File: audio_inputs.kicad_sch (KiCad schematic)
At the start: 14 parts, among them J2 PLR237/T10BK, U4 DIR9001PW

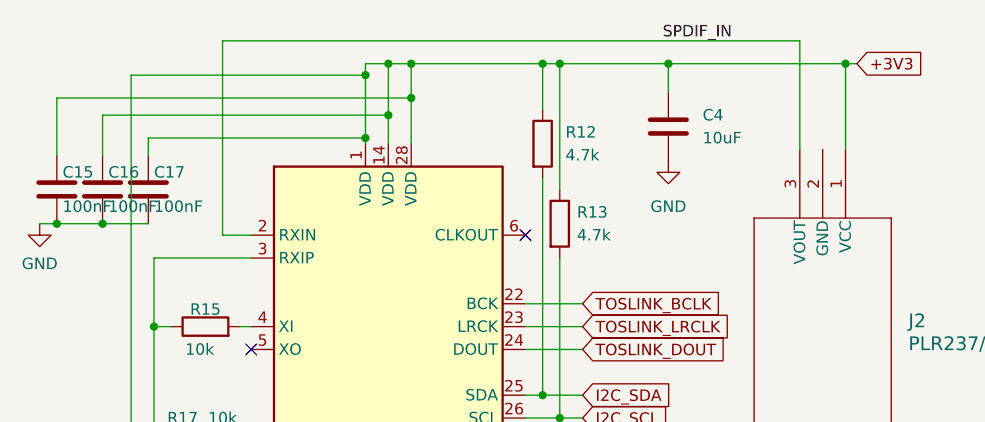
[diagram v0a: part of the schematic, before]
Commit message: Fixed RCA Jack symbols and footprints
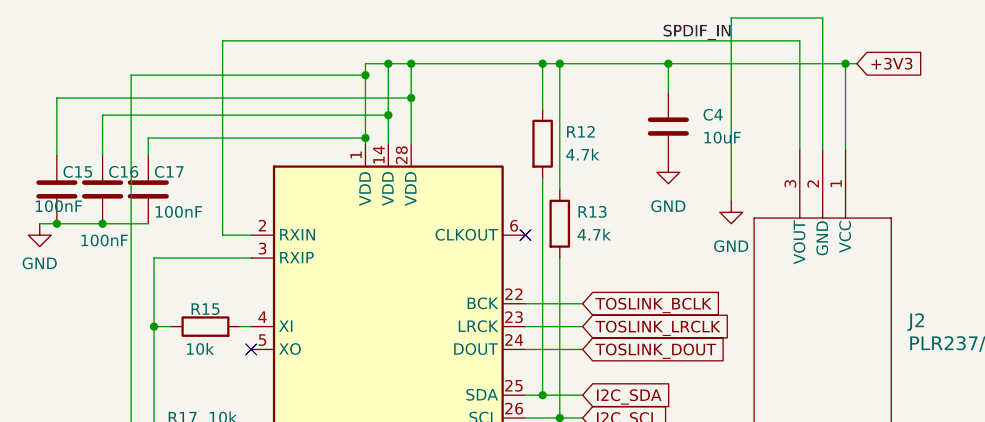
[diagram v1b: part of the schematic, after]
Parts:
- J2: footprint PLR237/T10BK_EVE -> Connector_Audio:PLR237-T10BK
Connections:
- net GND: now also J2.2 (GND)

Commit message: fixed cooper fill zone issue.  Fixed broken routes
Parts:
- J2: footprint Connector_Audio:PLR237-T10BK -> RCJ-042:PLR237T10BK
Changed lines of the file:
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@@
 			)
 		)
-		(property "Footprint" "Connector_Audio:PLR237-T10BK"
+		(property "Footprint" "RCJ-042:PLR237T10BK"
 			(at 136.525 57.785 0)
 			(effects

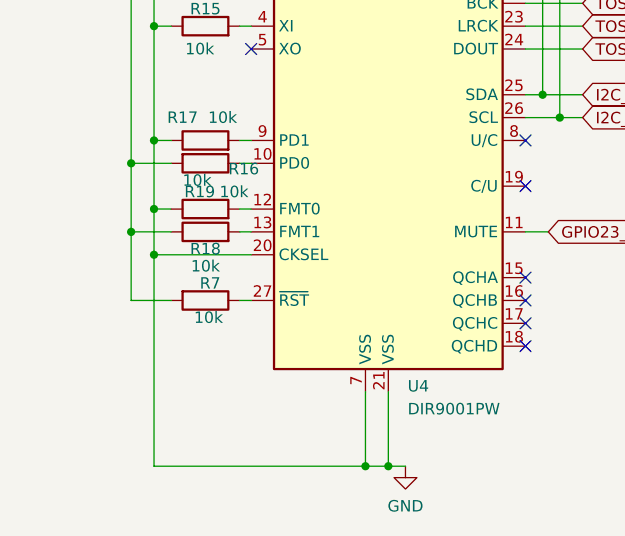
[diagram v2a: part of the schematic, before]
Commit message: Fixed inconsistencies in footprints and names
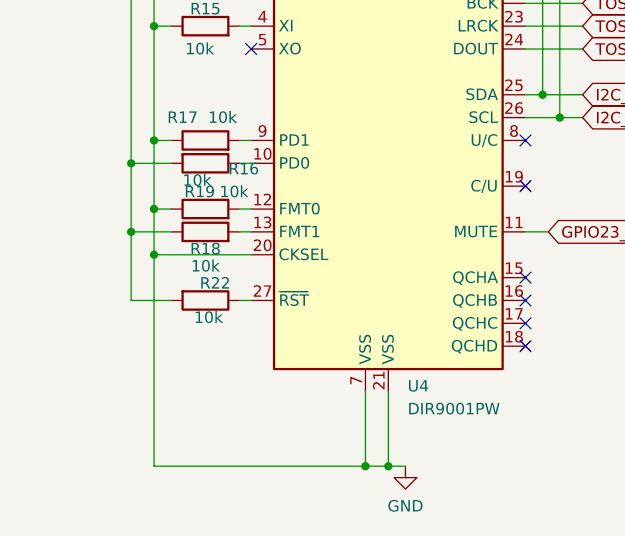
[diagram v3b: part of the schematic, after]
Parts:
- C4: footprint Resistor_SMD:R_0805_2012Metric_Pad1.20x1.40mm_HandSolder -> Capacitor_SMD:C_0805_2012Metric_Pad1.18x1.45mm_HandSolder
- renumbered R7 to R22
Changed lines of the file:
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@@
 		(on_board yes)
 		(dnp no)
-		(property "Reference" "R7"
+		(property "Reference" "R22"
 			(at 64.77 106.045 90)
 			(effects
@@
 			(project ""
 				(path "/e63e39d7-6ac0-4ffd-8aa3-1841a4541b55/69671d55-966b-4bba-8a79-dc8715674913"
-					(reference "R7")
+					(reference "R22")
 					(unit 1)
 				)
@@
 			)
 		)
-		(property "Footprint" "Resistor_SMD:R_0805_2012Metric_Pad1.20x1.40mm_HandSolder"
+		(property "Footprint" "Capacitor_SMD:C_0805_2012Metric_Pad1.18x1.45mm_HandSolder"
 			(at 117.8052 59.055 0)
 			(effects

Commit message: Removed unneeded crystal for DIR9001PW
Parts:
- U4: footprint Package_SO:SOIC-28W_7.5x17.9mm_P1.27mm -> Package_SO:TSSOP-28_4.4x9.7mm_P0.65mm
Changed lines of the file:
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@@
 			)
 		)
-		(property "Footprint" "Package_SO:SOIC-28W_7.5x17.9mm_P1.27mm"
+		(property "Footprint" "Package_SO:TSSOP-28_4.4x9.7mm_P0.65mm"
 			(at 85.725 119.38 0)
 			(effects

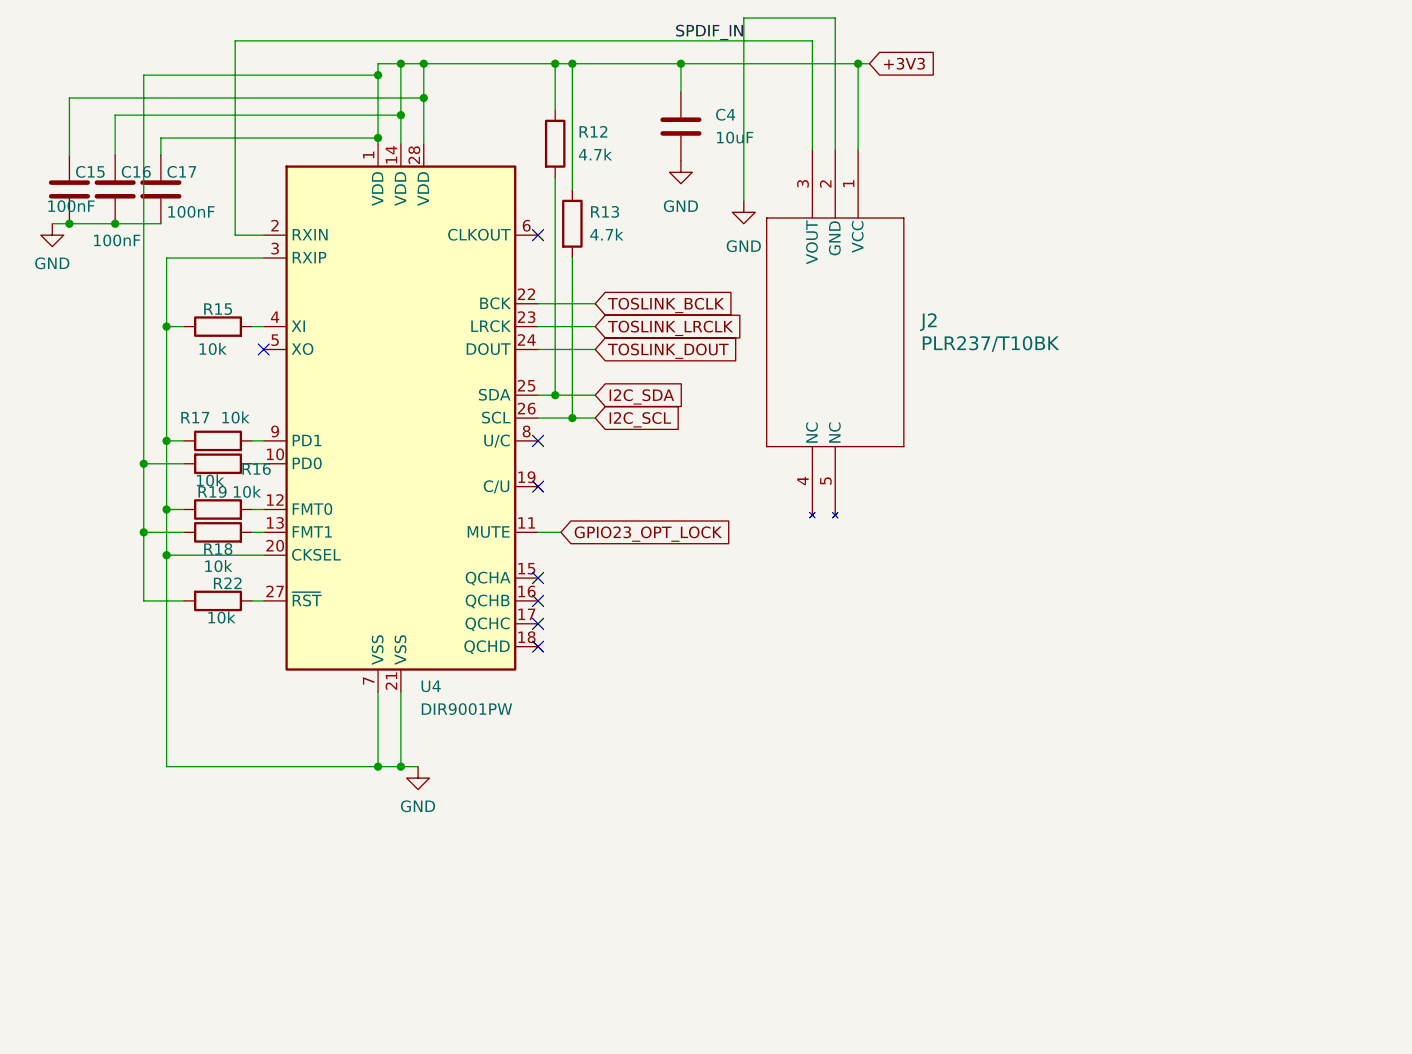
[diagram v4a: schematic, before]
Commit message: Updated schematic with correct symbol for DIR9001PW
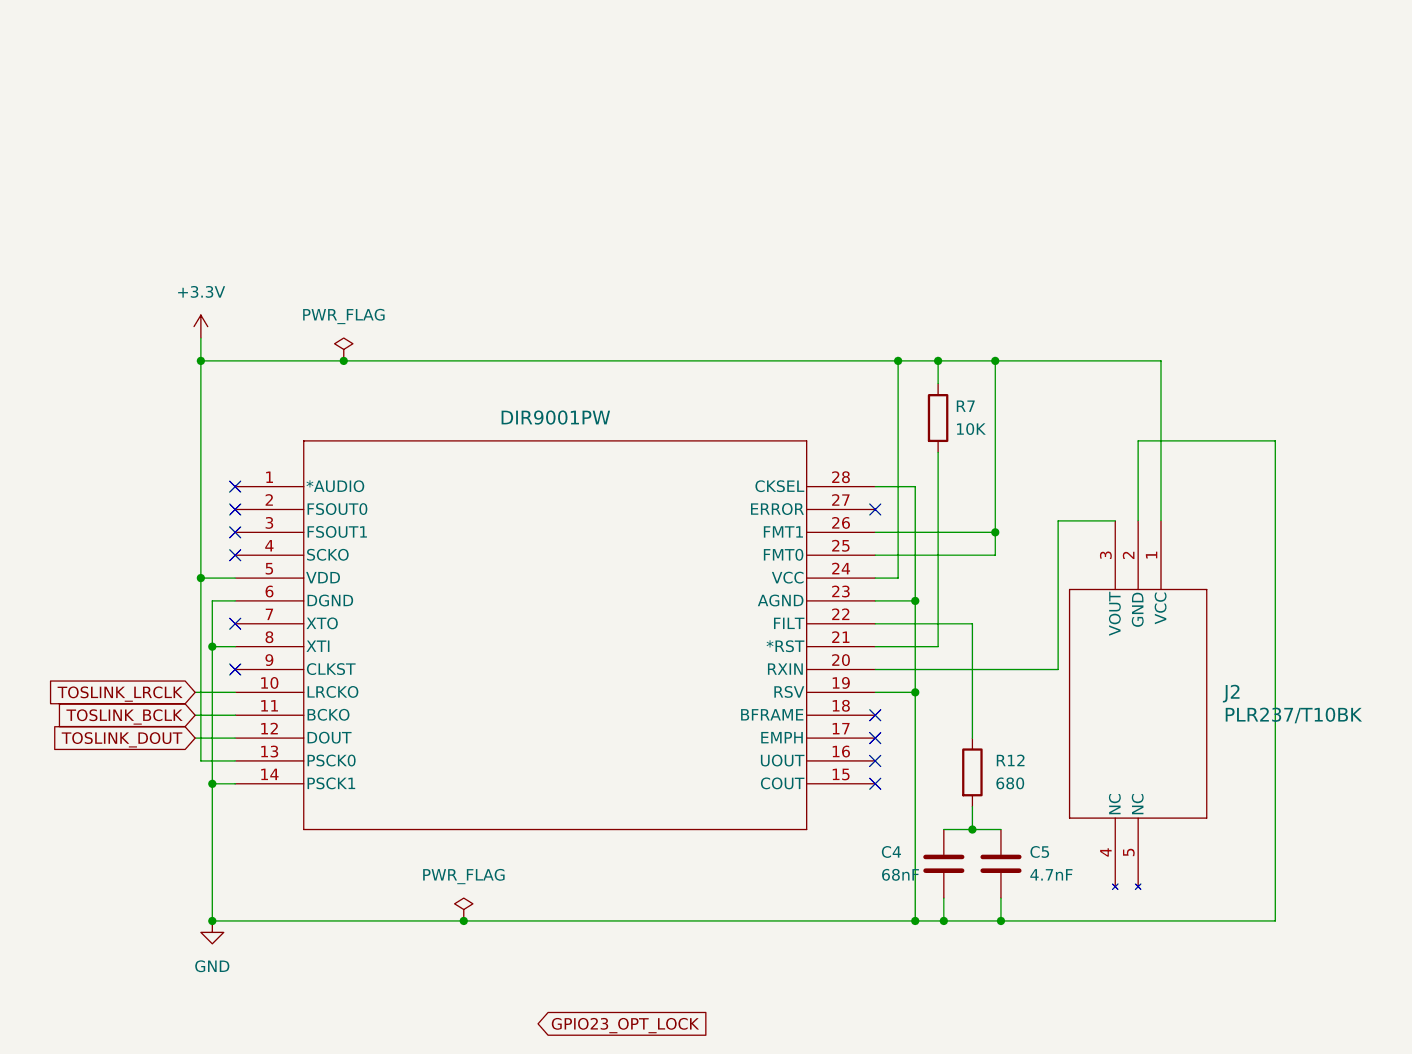
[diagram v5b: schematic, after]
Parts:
- removed C15, C16, C17: 100nF, Capacitor_SMD:C_0805_2012Metric_Pad1.18x1.45mm_HandSolder, symbol Device:C
- removed R13: 4.7k, Resistor_SMD:R_0805_2012Metric_Pad1.20x1.40mm_HandSolder, symbol Device:R
- removed R15, R16, R17, R18, R19, R22: 10k, Resistor_SMD:R_0805_2012Metric_Pad1.20x1.40mm_HandSolder, symbol Device:R
- removed U4: DIR9001PW, Package_SO:TSSOP-28_4.4x9.7mm_P0.65mm, symbol DIR9001:DIR9001PW
- added C5: 4.7nF, symbol Device:C
- added R7: 10K, symbol Device:R
- added U5: DIR9001PW, DIR9001_newfoot:PW28-M, symbol DIR9001:DIR9001PW
- C4: value 10uF -> 68nF; footprint Capacitor_SMD:C_0805_2012Metric_Pad1.18x1.45mm_HandSolder -> (none)
- R12: value 4.7k -> 680; footprint Resistor_SMD:R_0805_2012Metric_Pad1.20x1.40mm_HandSolder -> (none)
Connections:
- net GND: now also C5.2, U5.14 (PSCK1), U5.19 (RSV), U5.23 (AGND), U5.28 (CKSEL), U5.6 (DGND), U5.8 (XTI)
- net TOSLINK_BCLK: now also U5.11 (BCKO)
- net TOSLINK_DOUT: now also U5.12 (DOUT)
- net TOSLINK_LRCLK: now also U5.10 (LRCKO)
- removed net +3V3: C4.1, J2.1 (VCC), R12.1
- net I2C_SDA: no longer names the net of R12.2
- net I2C_SDA: now also C4.1, C5.1
- net SPDIF_IN: no longer names the net of J2.3 (VOUT)
- net SPDIF_IN: now also U5.20 (RXIN)
- new net: R7.2, U5.21 (*RST)
- new net: R12.1, U5.22 (FILT)
- new net +3.3V: J2.1 (VCC), R7.1, U5.13 (PSCK0), U5.24 (VCC), U5.25 (FMT0), U5.26 (FMT1), U5.5 (VDD)
- no-connect marks 8 -> 11
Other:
- moved on the sheet: J2

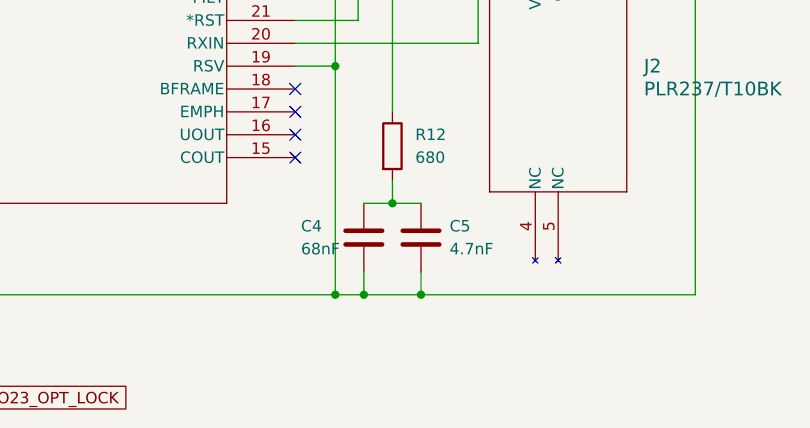
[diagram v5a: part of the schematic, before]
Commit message: Progress updating to correct footprint for DIR9001PW chip
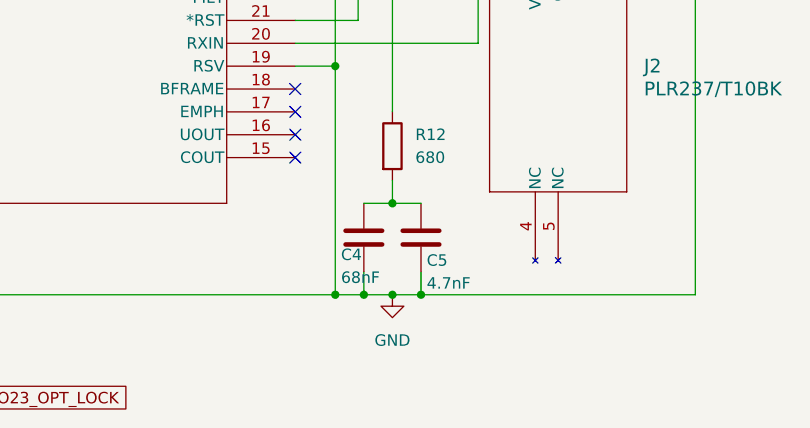
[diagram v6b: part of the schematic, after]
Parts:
- C4, C5: footprint (none) -> Capacitor_SMD:C_0805_2012Metric_Pad1.18x1.45mm_HandSolder
- R12, R7: footprint (none) -> Resistor_SMD:R_0805_2012Metric_Pad1.20x1.40mm_HandSolder
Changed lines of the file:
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@@
+	)
+	(junction
+		(at 149.225 143.51)
+		(diameter 0)
+		(color 0 0 0 0)
 	)
 	(junction
@@
 	(wire
 		(pts
-			(xy 146.05 143.51) (xy 152.4 143.51)
+			(xy 146.05 143.51) (xy 149.225 143.51)
 		)
 		(stroke
@@
 		(pts
 			(xy 92.71 143.51) (xy 142.875 143.51)
+		)
+		(stroke
+			(width 0)
+			(type default)
+		)
+	)
+	(wire
+		(pts
+			(xy 149.225 143.51) (xy 152.4 143.51)
 		)
 		(stroke
@@
 		(on_board yes)
 		(dnp no)
-		(fields_autoplaced yes)
 		(property "Reference" "#PWR06"
 			(at 64.77 149.86 0)
@@
 			)
 		)
-		(property "Footprint" ""
+		(property "Footprint" "Resistor_SMD:R_0805_2012Metric_Pad1.20x1.40mm_HandSolder"
 			(at 147.447 127 90)
 			(effects
@@
 			)
 		)
-		(property "Footprint" ""
+		(property "Footprint" "Resistor_SMD:R_0805_2012Metric_Pad1.20x1.40mm_HandSolder"
 			(at 143.637 87.63 90)
 			(effects
@@
 		(on_board yes)
 		(dnp no)
-		(fields_autoplaced yes)
 		(property "Reference" "C5"
-			(at 155.575 135.8899 0)
+			(at 153.035 139.7 0)
 			(effects
 				(font
@@
 		)
 		(property "Value" "4.7nF"
-			(at 155.575 138.4299 0)
+			(at 153.035 142.24 0)
 			(effects
 				(font
@@
 			)
 		)
-		(property "Footprint" ""
+		(property "Footprint" "Capacitor_SMD:C_0805_2012Metric_Pad1.18x1.45mm_HandSolder"
 			(at 153.3652 140.97 0)
 			(effects
@@
 				(path "/e63e39d7-6ac0-4ffd-8aa3-1841a4541b55/69671d55-966b-4bba-8a79-dc8715674913"
 					(reference "C5")
+					(unit 1)
+				)
+			)
+		)
+	)
+	(symbol
+		(lib_id "power:GND")
+		(at 149.225 143.51 0)
+		(unit 1)
+		(exclude_from_sim no)
+		(in_bom yes)
+		(on_board yes)
+		(dnp no)
+		(fields_autoplaced yes)
+		(property "Reference" "#PWR08"
+			(at 149.225 149.86 0)
+			(effects
+				(font
+					(size 1.27 1.27)
+				)
+				(hide yes)
+			)
+		)
+		(property "Value" "GND"
+			(at 149.225 148.59 0)
+			(effects
+				(font
+					(size 1.27 1.27)
+				)
+			)
+		)
+		(property "Footprint" ""
+			(at 149.225 143.51 0)
+			(effects
+				(font
+					(size 1.27 1.27)
+				)
+				(hide yes)
+			)
+		)
+		(property "Datasheet" ""
+			(at 149.225 143.51 0)
+			(effects
+				(font
+					(size 1.27 1.27)
+				)
+				(hide yes)
+			)
+		)
+		(property "Description" "Power symbol creates a global label with name \"GND\" , ground"
+			(at 149.225 143.51 0)
+			(effects
+				(font
+					(size 1.27 1.27)
+				)
+				(hide yes)
+			)
+		)
+		(pin "1"
+		)
+		(instances
+			(project ""
+				(path "/e63e39d7-6ac0-4ffd-8aa3-1841a4541b55/69671d55-966b-4bba-8a79-dc8715674913"
+					(reference "#PWR08")
 					(unit 1)
 				)
@@
 		(dnp no)
 		(property "Reference" "C4"
-			(at 139.065 135.89 0)
+			(at 143.51 139.065 0)
 			(effects
 				(font
@@
 		)
 		(property "Value" "68nF"
-			(at 139.065 138.43 0)
+			(at 143.51 141.605 0)
 			(effects
 				(font
@@
 			)
 		)
-		(property "Footprint" ""
+		(property "Footprint" "Capacitor_SMD:C_0805_2012Metric_Pad1.18x1.45mm_HandSolder"
 			(at 147.0152 140.97 0)
 			(effects

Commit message: kinda broken
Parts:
- renumbered C4 to C18, C5 to C19
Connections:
- net TOSLINK Error: now reaches U5.27 (ERROR)
- no-connect marks 11 -> 10
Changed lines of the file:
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@@
-	)
-	(no_connect
-		(at 138.43 97.79)
 	)
 	(no_connect
@@
 	(wire
 		(pts
-			(xy 158.75 115.57) (xy 158.75 99.06)
+			(xy 156.845 115.57) (xy 156.845 99.06)
 		)
 		(stroke
@@
 	(wire
 		(pts
-			(xy 138.43 115.57) (xy 158.75 115.57)
+			(xy 138.43 115.57) (xy 156.845 115.57)
 		)
 		(stroke
@@
 	(wire
 		(pts
-			(xy 158.75 99.06) (xy 165.1 99.06)
+			(xy 156.845 99.06) (xy 165.1 99.06)
 		)
 		(stroke
@@
 	(wire
 		(pts
+			(xy 138.43 97.79) (xy 140.335 97.79)
+		)
+		(stroke
+			(width 0)
+			(type default)
+		)
+	)
+	(wire
+		(pts
 			(xy 149.225 143.51) (xy 152.4 143.51)
 		)
@@
 			(width 0)
 			(type default)
-		)
-	)
-	(global_label "GPIO23_OPT_LOCK"
-		(shape input)
-		(at 100.965 154.94 0)
-		(fields_autoplaced yes)
-		(effects
-			(font
-				(size 1.27 1.27)
-			)
-			(justify left)
-		)
-		(property "Intersheetrefs" "${INTERSHEET_REFS}"
-			(at 121.3415 154.94 0)
-			(effects
-				(font
-					(size 1.27 1.27)
-				)
-				(justify left)
-				(hide yes)
-			)
 		)
 	)
@@
 				)
 				(justify right)
+				(hide yes)
+			)
+		)
+	)
+	(global_label "TOSLINK Error"
+		(shape input)
+		(at 140.335 97.79 0)
+		(fields_autoplaced yes)
+		(effects
+			(font
+				(size 1.27 1.27)
+			)
+			(justify left)
+		)
+		(property "Intersheetrefs" "${INTERSHEET_REFS}"
+			(at 156.7805 97.79 0)
+			(effects
+				(font
+					(size 1.27 1.27)
+				)
+				(justify left)
 				(hide yes)
 			)
@@
 		(on_board yes)
 		(dnp no)
-		(property "Reference" "C5"
+		(property "Reference" "C19"
 			(at 153.035 139.7 0)
 			(effects
@@
 			(project ""
 				(path "/e63e39d7-6ac0-4ffd-8aa3-1841a4541b55/69671d55-966b-4bba-8a79-dc8715674913"
-					(reference "C5")
+					(reference "C19")
 					(unit 1)
 				)
@@
 		(on_board yes)
 		(dnp no)
-		(property "Reference" "C4"
+		(property "Reference" "C18"
 			(at 143.51 139.065 0)
 			(effects
@@
 			(project ""
 				(path "/e63e39d7-6ac0-4ffd-8aa3-1841a4541b55/69671d55-966b-4bba-8a79-dc8715674913"
-					(reference "C4")
+					(reference "C18")
 					(unit 1)
 				)
